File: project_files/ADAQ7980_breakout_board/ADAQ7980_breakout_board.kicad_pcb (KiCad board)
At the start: 2 copper layers, 30 x 20 mm, 14 parts, among them J1 Conn_01x06, J2 Conn_01x06, J3 Conn_01x02

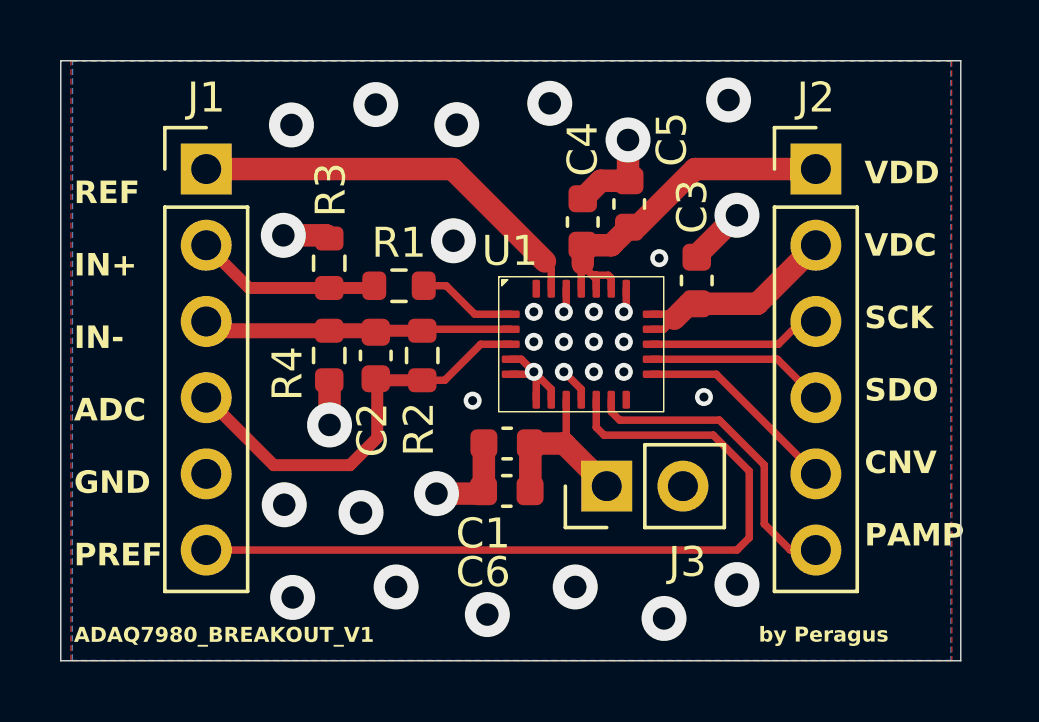
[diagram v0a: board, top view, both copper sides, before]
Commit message: Changed names of !PD pins to the correct ones
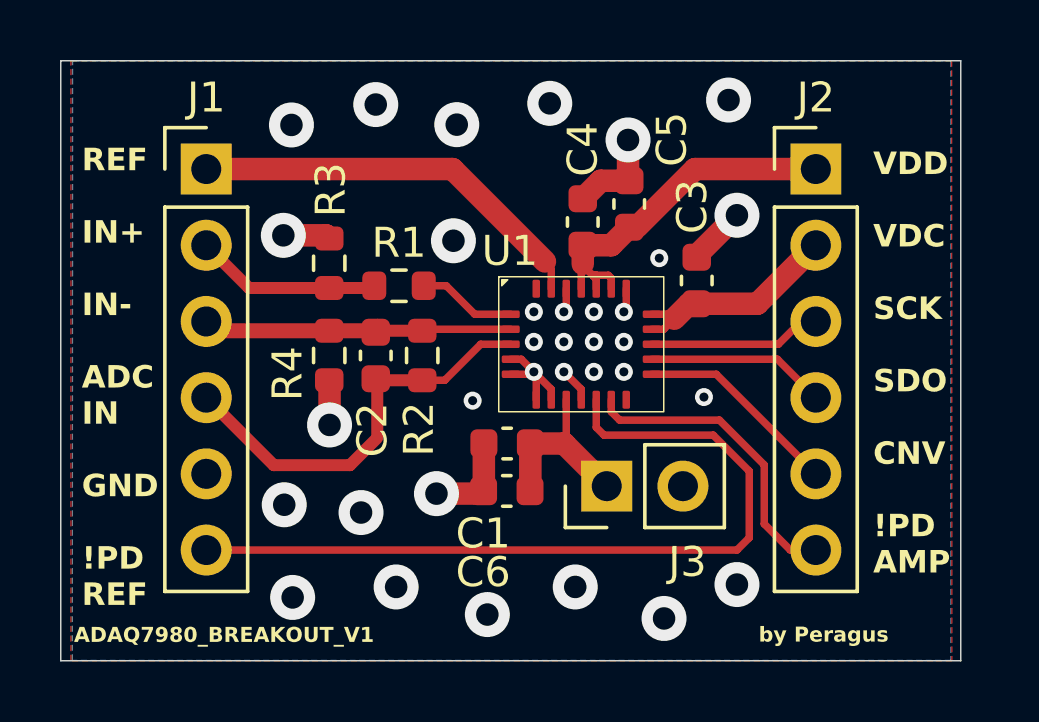
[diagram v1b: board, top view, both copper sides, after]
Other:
- board text added: "REF IN+ IN- ADC IN GND !PD REF"
- board text added: "VDD VDC SCK SDO CNV !PD AMP"
- board text removed: "REF IN+ IN- ADC GND PREF"
- board text removed: "VDD VDC SCK SDO CNV PAMP"
